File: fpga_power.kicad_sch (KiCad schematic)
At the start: 0 parts

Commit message: develop: Deleted FPGA_XCVR because there are no xcvrs on this part. Updated symbol.
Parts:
- added U4: ~, symbol duality:TI60F225

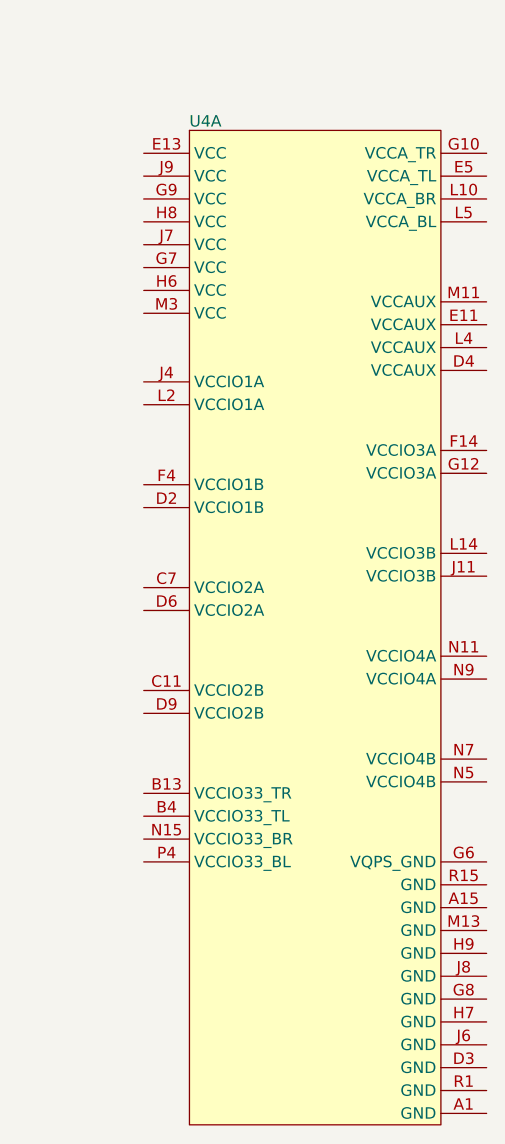
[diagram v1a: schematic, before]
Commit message: develop: Added 1.8/3.3V and 0.95V power regulators.
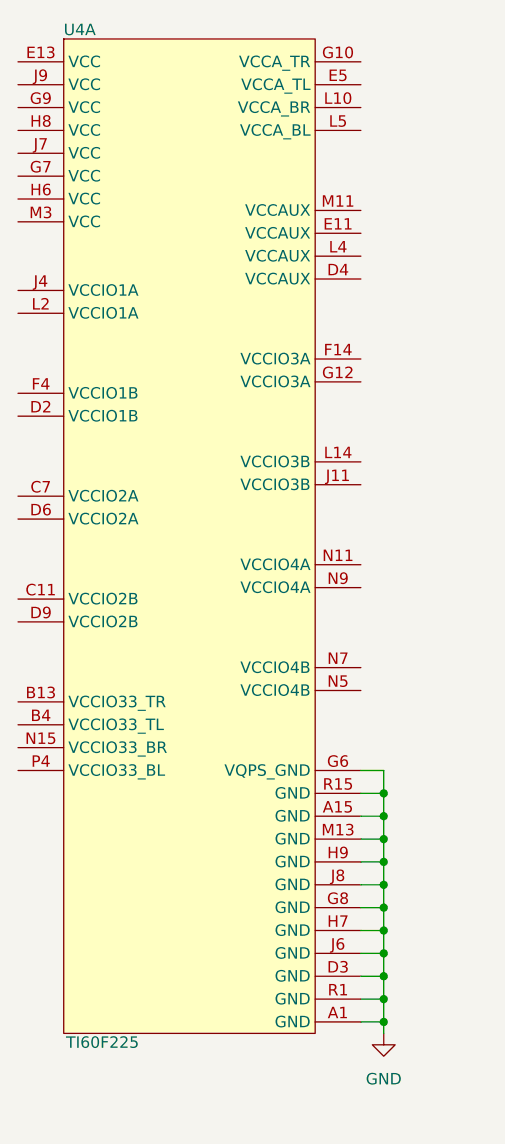
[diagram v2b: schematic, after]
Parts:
- U4: value ~ -> TI60F225; footprint (none) -> duality:BGA-225_15x15_10.0x10.0
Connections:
- net GND: now reaches U4.A1 (GND)
- net GND: now also U4.A15 (GND), U4.D3 (GND), U4.G6 (VQPS_GND), U4.G8 (GND), U4.H7 (GND), U4.H9 (GND), U4.J6 (GND), U4.J8 (GND), U4.M13 (GND), U4.R1 (GND), U4.R15 (GND)
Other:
- moved on the sheet: U4A
